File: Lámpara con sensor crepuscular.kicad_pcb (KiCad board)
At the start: 2 copper layers, 64.2 x 18.2 mm, 9 parts, among them J1 NA COM NC, J2 +12V GND, K1 G5LE-1, Q1 BC547

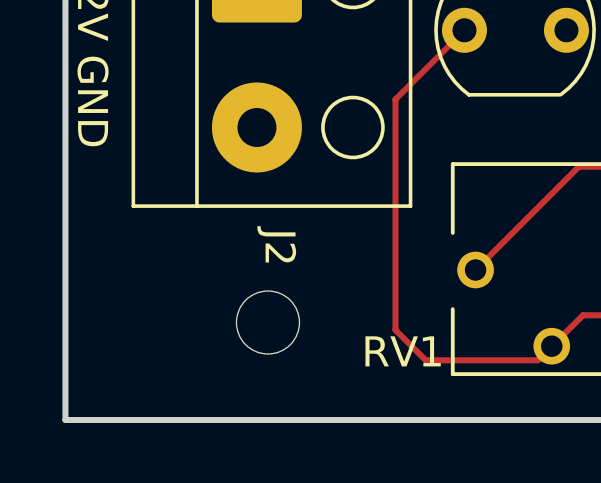
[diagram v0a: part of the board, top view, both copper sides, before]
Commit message: Añadir carpetas para guardar los archivos gerber, POS y BOM organizados por carpetas, hacer un README correspondiente al proyecto, colocar imagenes y videos referentes al proyecto como visualización en 3D, Esquemático y simulación del circuito
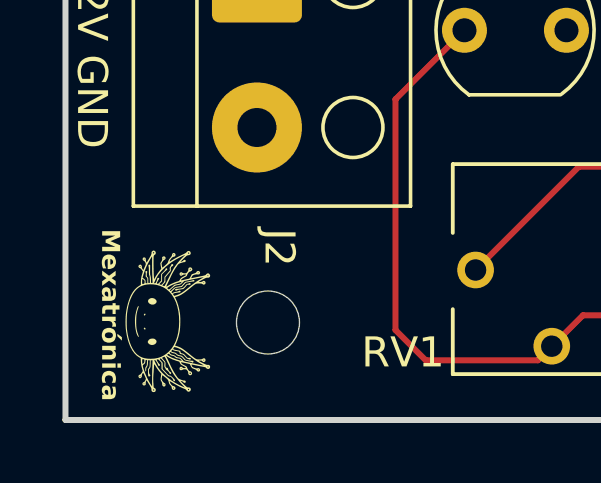
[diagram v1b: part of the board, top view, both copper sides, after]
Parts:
- added G***: Mexatrónica, Archivos extra de huellas:Logo Mexatronica Huella 05mm, F.Cu at (126.0, 82.5)
